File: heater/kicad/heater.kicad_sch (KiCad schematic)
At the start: 77 parts, among them J1 Conn_01x02_Pin, J2 Conn_01x02_Pin, J5 pcie_98, U1 ADS1261BIRHBT, U10 B0509XT-1WR3, U14 OPA333, U15 LTC1968, U16 OPA333, U2 ESD5344D-TP, U3 XC6206P332MR, U4 TPS7A2050PDBVR, U5 ADuM120N, U6 ADuM120N, U7 ADuM120N, U9 XC6206P332MR

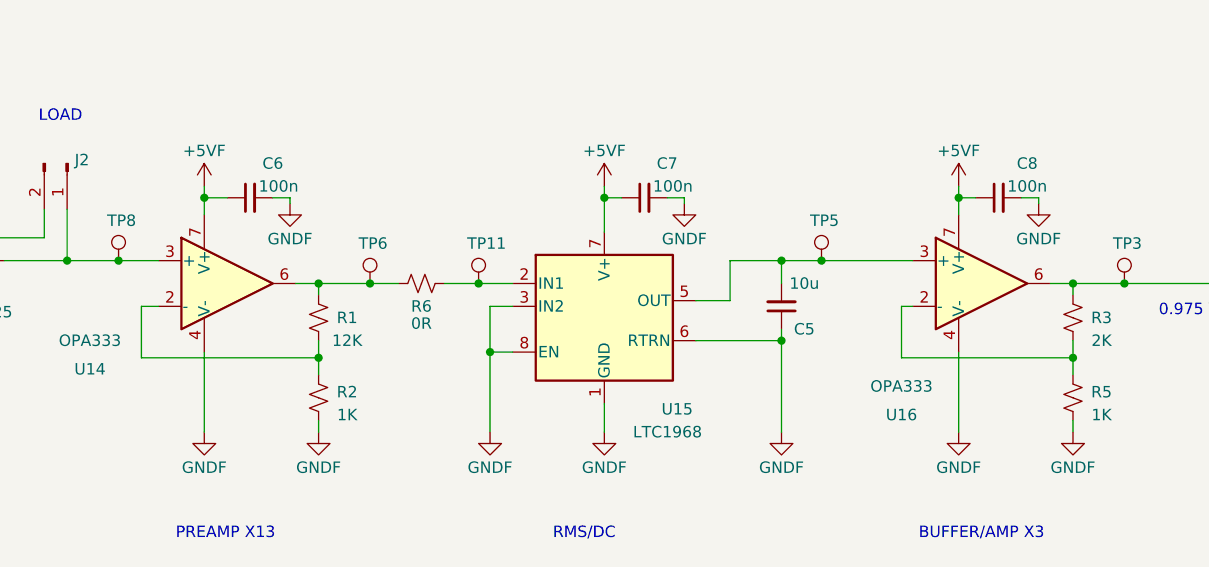
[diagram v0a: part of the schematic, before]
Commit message: Updated OPA333 pinout
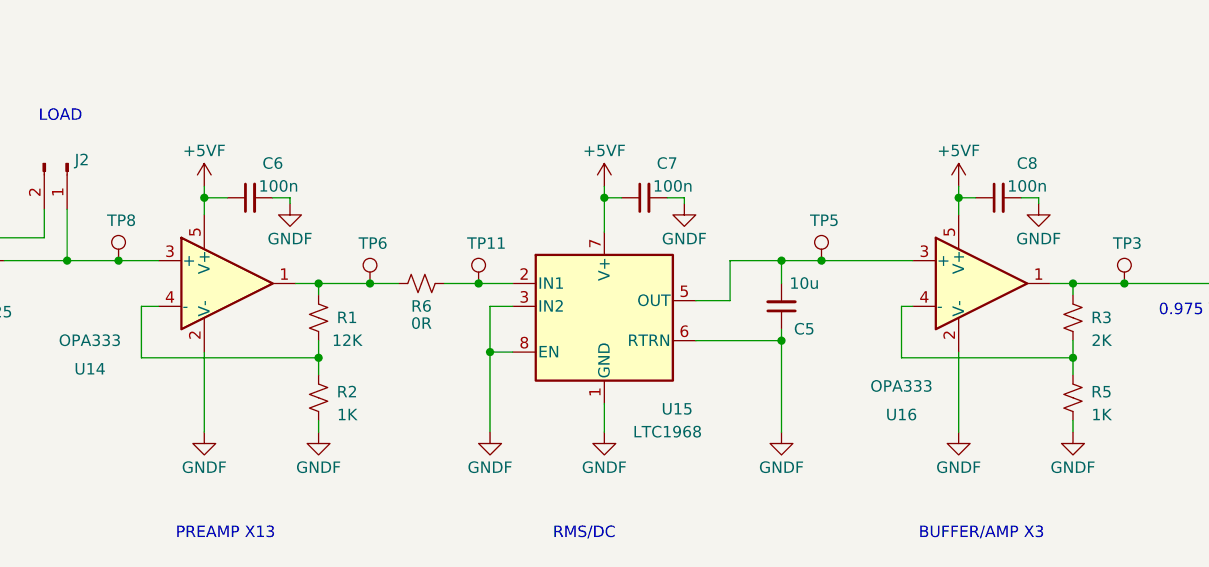
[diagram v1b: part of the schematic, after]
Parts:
- U14, U16: footprint Package_SO:SOIC-8_3.9x4.9mm_P1.27mm -> heater:SOT-23-5; symbol Amplifier_Operational:OPA333xxD -> Amplifier_Operational:OPA330xxDBV
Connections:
- net +5V: now also U14.5 (V+), U16.5 (V+); no longer U14.7 (V+), U16.7 (V+)
- net GND1: now also U14.2 (V-), U16.2 (V-); no longer U14.4 (V-), U16.4 (V-)
- net ISENSE: now also U16.1; no longer U16.6
- net at U14.1: now also R1.2, R6.2, TP6.1
- net at R1.1, R2.2: now also U14.4 (-); no longer U14.2 (-)
- net at R3.1, R5.2: now also U16.4 (-); no longer U16.2 (-)
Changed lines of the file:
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@@
     )
   )
-  (symbol (lib_id "Amplifier_Operational:OPA333xxD") (at 92.075 75.565 0) (unit 1)
+  (symbol (lib_id "Amplifier_Operational:OPA330xxDBV") (at 92.075 75.565 0) (unit 1)
     (in_bom yes) (on_board yes) (dnp no)
     (property "Reference" "U14" (at 76.835 85.09 0)
@@
       (effects (font (size 1.27 1.27)))
     )
-    (property "Footprint" "Package_SO:SOIC-8_3.9x4.9mm_P1.27mm" (at 89.535 80.645 0)
+    (property "Footprint" "heater:SOT-23-5" (at 89.535 80.645 0)
       (effects (font (size 1.27 1.27)) (justify left) hide)
     )
-    (property "Datasheet" "http://www.ti.com/lit/ds/symlink/opa333.pdf" (at 95.885 71.755 0)
-      (effects (font (size 1.27 1.27)) hide)
-    )
-    (pin "1")
-    (pin "2")
+    (property "Datasheet" "http://www.ti.com/lit/ds/symlink/opa330.pdf" (at 92.075 70.485 0)
+      (effects (font (size 1.27 1.27)) hide)
+    )
+    (pin "2")
+    (pin "5")
+    (pin "1")
     (pin "3")
     (pin "4")
-    (pin "5")
-    (pin "6")
-    (pin "7")
-    (pin "8")
     (instances
       (project "heater"
@@
     )
   )
-  (symbol (lib_id "Amplifier_Operational:OPA333xxD") (at 175.895 75.565 0) (unit 1)
+  (symbol (lib_id "Amplifier_Operational:OPA330xxDBV") (at 175.895 75.565 0) (unit 1)
     (in_bom yes) (on_board yes) (dnp no)
     (property "Reference" "U16" (at 167.005 90.17 0)
@@
       (effects (font (size 1.27 1.27)))
     )
-    (property "Footprint" "Package_SO:SOIC-8_3.9x4.9mm_P1.27mm" (at 173.355 80.645 0)
+    (property "Footprint" "heater:SOT-23-5" (at 173.355 80.645 0)
       (effects (font (size 1.27 1.27)) (justify left) hide)
     )
-    (property "Datasheet" "http://www.ti.com/lit/ds/symlink/opa333.pdf" (at 179.705 71.755 0)
-      (effects (font (size 1.27 1.27)) hide)
-    )
-    (pin "1")
-    (pin "2")
+    (property "Datasheet" "http://www.ti.com/lit/ds/symlink/opa330.pdf" (at 175.895 70.485 0)
+      (effects (font (size 1.27 1.27)) hide)
+    )
+    (pin "2")
+    (pin "5")
+    (pin "1")
     (pin "3")
     (pin "4")
-    (pin "5")
-    (pin "6")
-    (pin "7")
-    (pin "8")
-    (instances
-      (project "heater"
+    (instances
+      (project "heater"

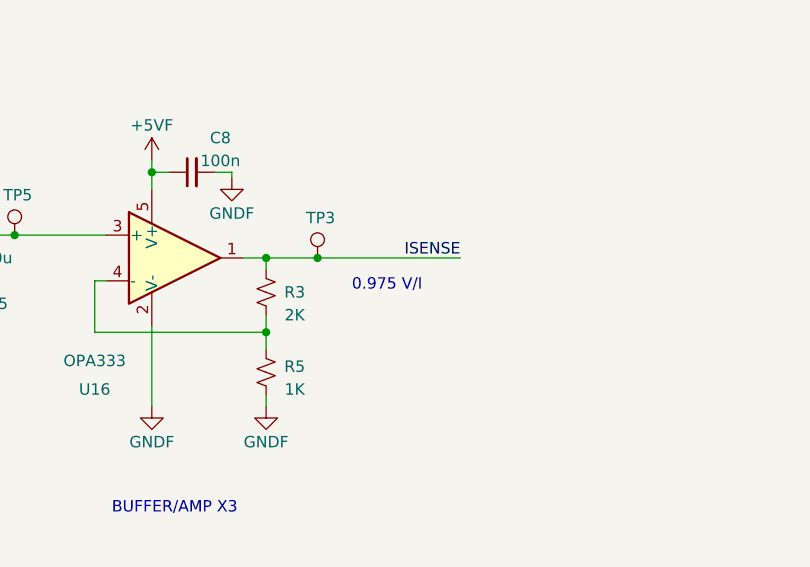
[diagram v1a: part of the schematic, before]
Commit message: Updated the heater schematic.
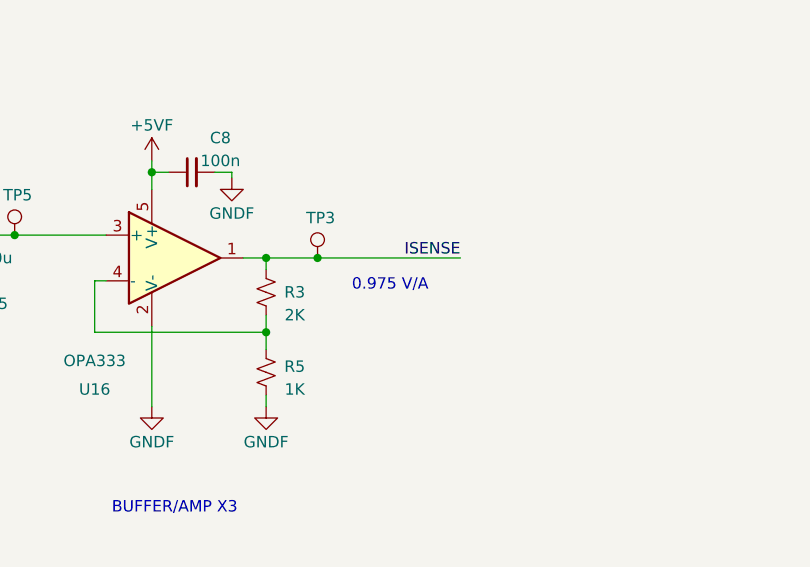
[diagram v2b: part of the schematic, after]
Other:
- note added: "0.975 V/A"
- note removed: "0.975 V/I"
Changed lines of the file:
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@@
     (effects (font (size 1.27 1.27)) (justify left bottom))
   )
-  (text "0.975 V/I" (at 195.58 79.375 0)
+  (text "0.975 V/A" (at 195.58 79.375 0)
     (effects (font (size 1.27 1.27)) (justify left bottom))
   )

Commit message: Updated heater schematic.
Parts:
- removed C12, C13, C30, C31, C44: 100n, Capacitor_SMD:C_0402_1005Metric, symbol Device:C_Small
- removed C17: 4n7, Capacitor_SMD:C_0402_1005Metric, symbol Device:C_Small
- removed C21, C35: 1u, Capacitor_SMD:C_0402_1005Metric, symbol Device:C_Small
- removed C22, C29, C32: 10u, Capacitor_SMD:C_0603_1608Metric, symbol Device:C_Small
- removed D3, D4: GRN, LED_SMD:LED_0603_1608Metric, symbol Device:LED
- removed R16, R28, R29: 51K, Resistor_SMD:R_0402_1005Metric, symbol Device:R_Small_US
- removed R18, R19, R21, R22: 47R, Resistor_SMD:R_0402_1005Metric, symbol Device:R_Small_US
- removed R24: 10K, Resistor_SMD:R_0402_1005Metric, symbol Device:R_Small_US
- removed R25, R26: 5K1, Resistor_SMD:R_0402_1005Metric, symbol Device:R_Small_US
- removed U1: ADS1261BIRHBT, heater:RHB0032E, symbol heater:ADS1261IRHBR
- removed U5, U6, U7: ADuM120N, Package_SO:SOIC-8_3.9x4.9mm_P1.27mm, symbol Isolator:ADuM120N
- removed U9: XC6206P332MR, Package_TO_SOT_SMD:SOT-23-3, symbol breakout:XC6206P332MR
- added C15, C16: 100n, Capacitor_SMD:C_0402_1005Metric, symbol Device:C_Small
- added R10, R7, R8, R9: ~, Resistor_SMD:R_0402_1005Metric, symbol Device:R_Small_US
- added R11: 12K, symbol Device:R_Small_US
- added R12: 1K, symbol Device:R_Small_US
- added U1: OPA333, heater:SOT-23-5, symbol Amplifier_Operational:OPA330xxDBV
- added U5: ISO1541, Package_SO:SOIC-8_3.9x4.9mm_P1.27mm, symbol Isolator:ISO1541
- added U8: ADS1115IDGS, Package_SO:TSSOP-10_3x3mm_P0.5mm, symbol heater:ADS1115IDGS
- C10, C11: value 1u -> 100n; LCSC C52923 -> C1525
- R15: value 51K -> 5K1; LCSC C25794 -> C25905
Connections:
- net +2V5A is gone; now on net +3V3: C10.2
- net +5VD is gone; now on net +5V: C1.2, C2.2, J5.B1 (Pin_b1), J5.B2 (Pin_b2), J5.B3 (Pin_b3), J5.B4 (Pin_b4), U3.3 (VIN)
- net +5V: now also U2.4 (D3), U2.5 (D4); no longer C24.2, C26.2, C27.2, C28.2, C6.1, C7.1, C8.1, C9.2, TP4.1, TP7.1, TP9.1, U10.5 (VOUT), U14.5 (V+), U15.7 (V+), U16.5 (V+), U4.1 (IN), U4.3 (EN), U4.5 (OUT)
- net GND: now also D2.1 (K), U5.4 (GND1); no longer C11.2, D1.1 (K), D2.2 (A), D5.1 (K)
- net GND1: now also C11.2, D1.1 (K), D5.1 (K), C15.2, C16.2, R12.1, U1.2 (V-), U5.5 (GND2), U8.1 (ADDR), U8.3 (GND)
- net +3V3: now reaches R15.1
- net +3V3: now also C3.2, C4.2, TP2.1, U3.2 (VOUT), U5.1 (VCC1)
- net PB7: now reaches U2.1 (D1)
- net PB7: now also J5.B7 (Pin_b7), R9.1, U5.2 (SDA1)
- net PB8: now reaches U2.2 (D2)
- net PB8: now also J5.B8 (Pin_b8), R10.1, U5.3 (SCL1)
- removed net +3V3D: C11.1, C3.2, C4.2, R15.2, R27.1, TP2.1, U3.2 (VOUT)
- net +5VA: no longer names the net of R23.1
- net +5VA: now also TP9.1, U1.1
- net ISENSE: no longer names the net of R3.2, TP3.1, U16.1
- net ISENSE: now also U1.3 (+), U8.4 (AIN0)
- net PA5: no longer names the net of J5.B28 (Pin_b28)
- net PA6: no longer names the net of J5.B21 (Pin_b21)
- net PA7: no longer names the net of J5.A27 (Pin_a27)
- net PB14: no longer names the net of J5.A16 (Pin_a16)
- new net: R8.1, U5.6 (SCL2), U8.10 (SCL)
- new net: R11.1, R12.2, U1.4 (-)
- new net: D2.2 (A), R15.2
- new net: R7.1, U5.7 (SDA2), U8.9 (SDA)
- new net +5VF: C11.1, C15.1, C16.1, C27.2, C28.2, C6.1, C7.1, C8.1, R10.2, R11.2, R27.1, R7.2, R8.2, R9.2, TP7.1, U1.5 (V+), U14.5 (V+), U15.7 (V+), U16.5 (V+), U4.5 (OUT), U5.8 (VCC2), U8.8 (VDD)
- new net 9VF: C24.2, C26.2, C9.2, TP4.1, U10.5 (VOUT), U4.1 (IN), U4.3 (EN)
- no-connect marks 92 -> 93
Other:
- note added: "CURRENT DETECTOR"
- note added: "LOW NOISE 5V"
- note added: "PWM CURRENT SENSOR"
- note added: "TODO: ADD PWD digital output."
- note added: "TODO: Add ADC addressing."
- note added: "TODO: Add test points"
- note added: "TODO: Change full scale to 4A."
- note added: "TODO: Consider adding a filter between analog and digital 5VF."
- note added: "TODO: Revisit bypass capacitors"
- note removed: "0.975 V/A"
- note removed: "ANALOG LOW NOISE 5V"
- note removed: "DIGITAL 3.3V"
- note removed: "TODO: Add DC/DC capacitors."
- moved on the sheet: C1, C14, C2, C24, C26, C27, C28, C3, C4, C5, C6, C7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

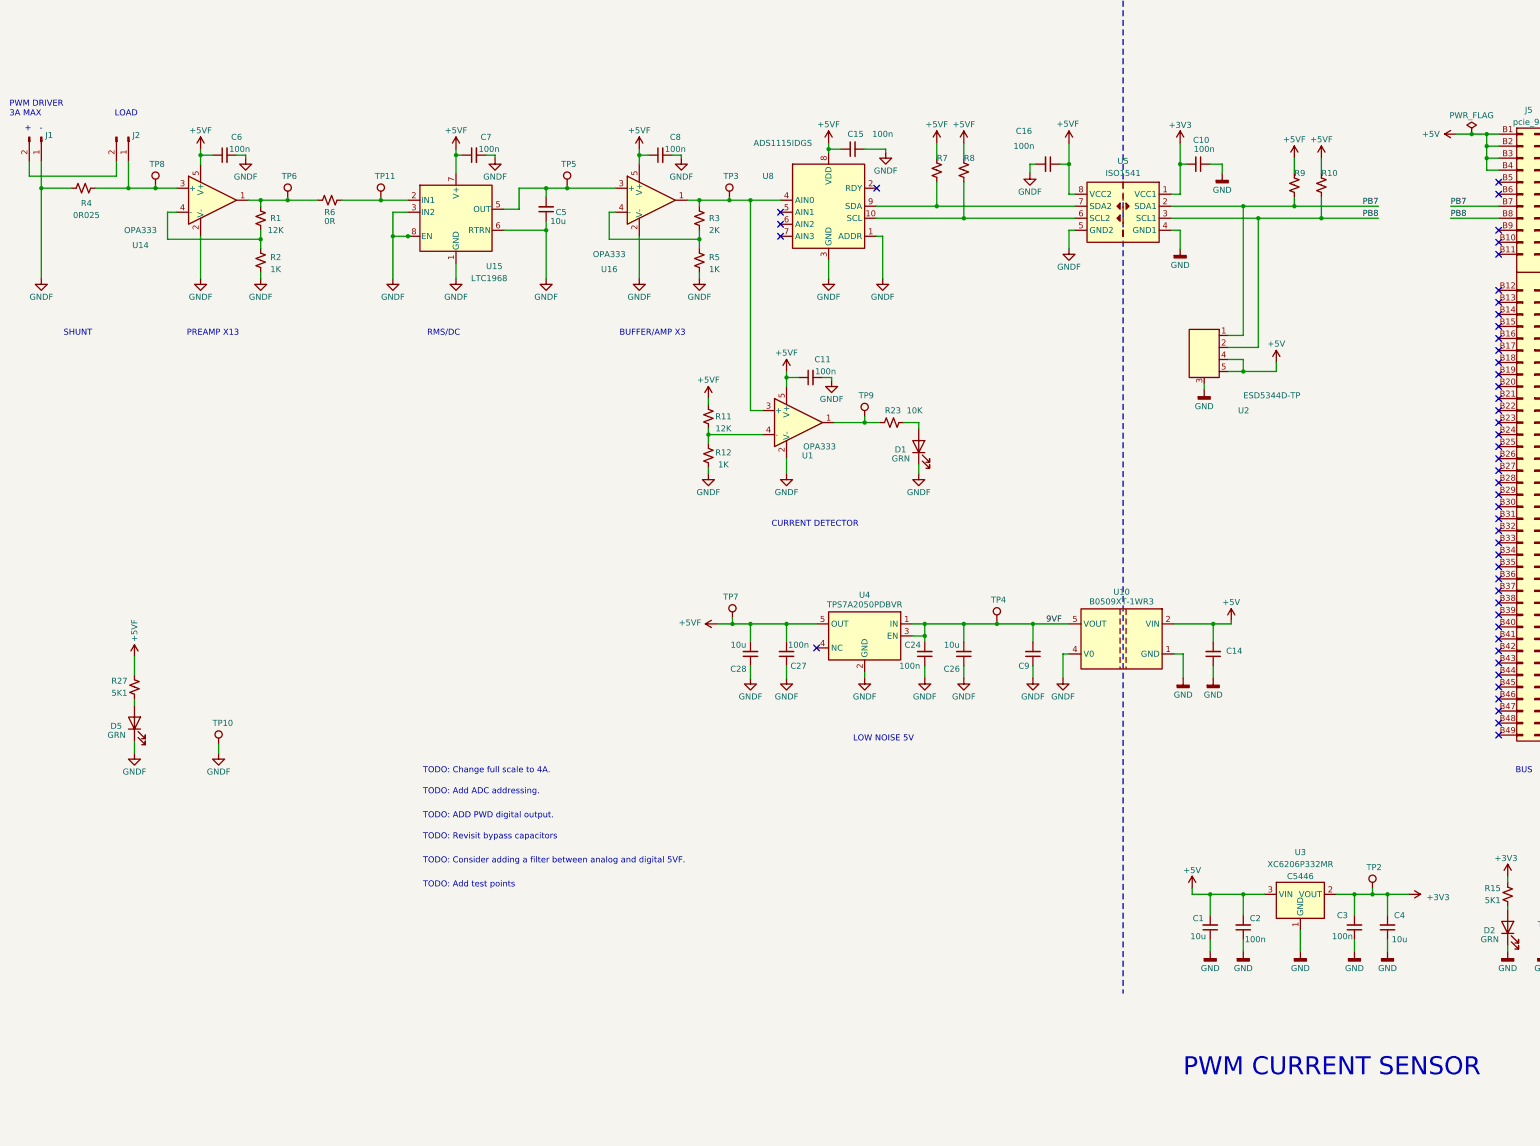
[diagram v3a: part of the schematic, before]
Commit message: Updated heater schematic
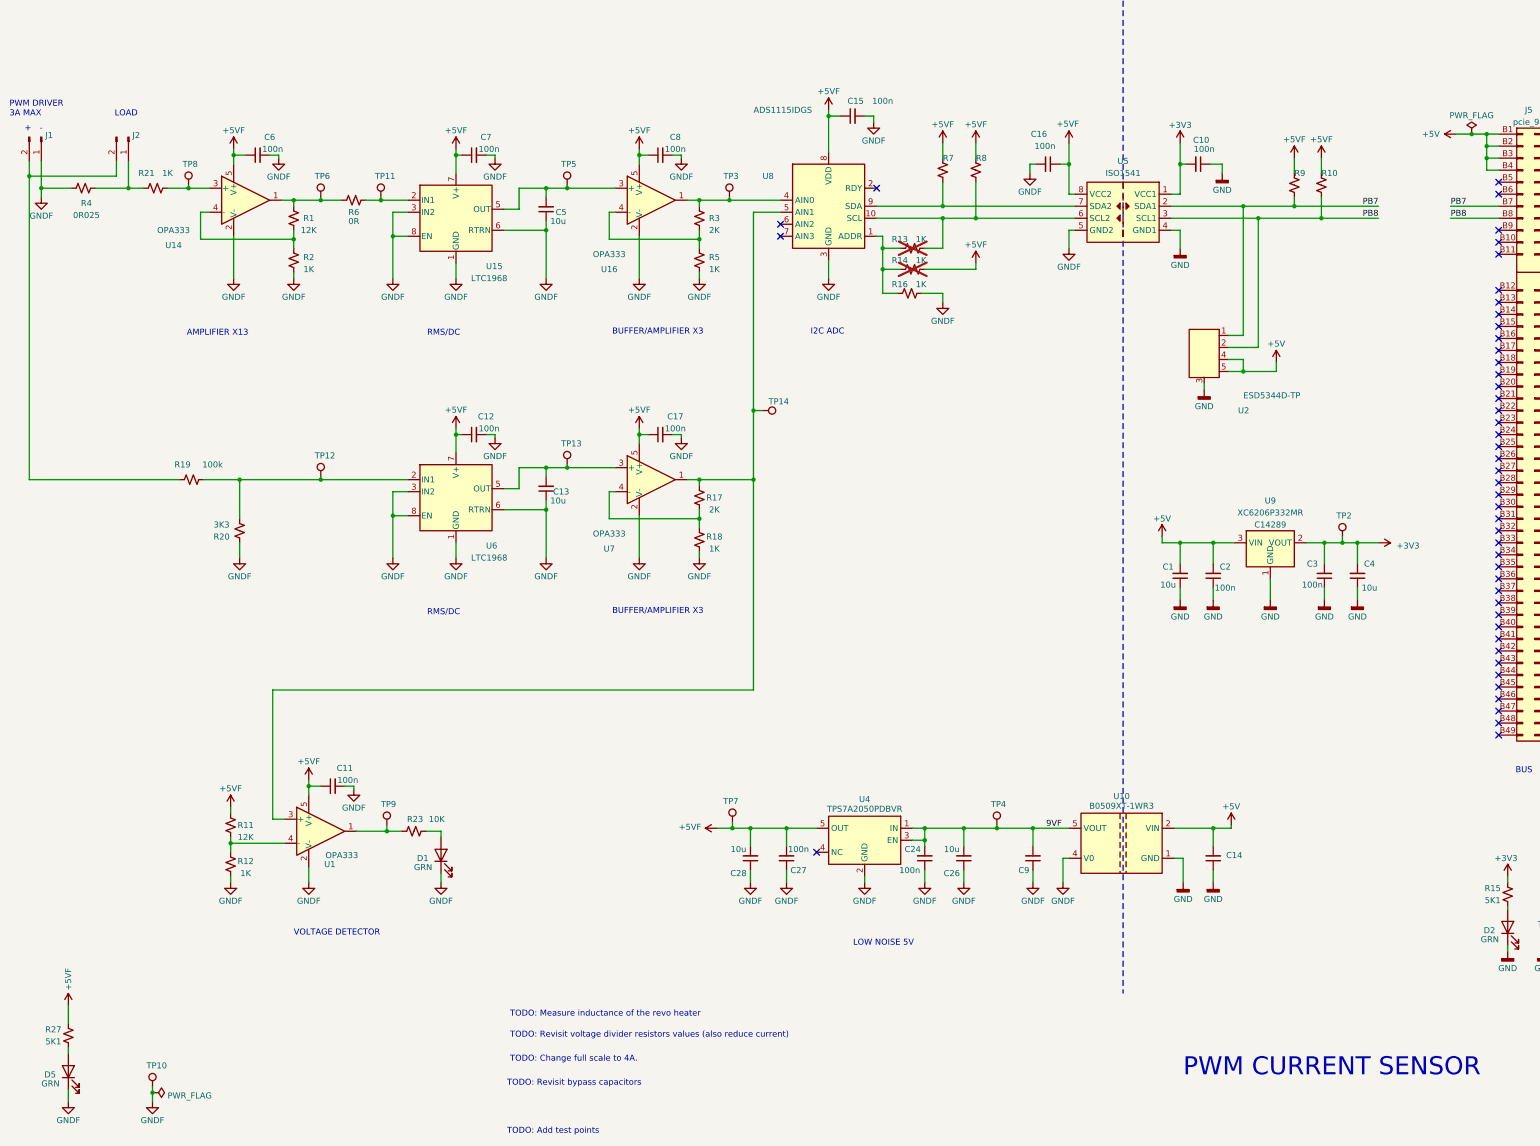
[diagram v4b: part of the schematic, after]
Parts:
- removed U3: XC6206P332MR, Package_TO_SOT_SMD:SOT-23-3, symbol breakout:XC6206P332MR
- added C12, C17: 100n, Capacitor_SMD:C_0402_1005Metric, symbol Device:C_Small
- added C13: 10u, Capacitor_SMD:C_0603_1608Metric, symbol Device:C_Small
- added R13, R14, R16: 1K, Resistor_SMD:R_0402_1005Metric, symbol Device:R_Small_US
- added R17: 2K, Resistor_SMD:R_0402_1005Metric, symbol Device:R_Small_US
- added R18, R21: 1K, symbol Device:R_Small_US
- added R19: 100k, symbol Device:R_Small_US
- added R20: 3K3, symbol Device:R_Small_US
- added TP12, TP13, TP14: TestPoint, common:Test_Pad, symbol common:TestPoint
- added U6: LTC1968, symbol heater:LTC1968
- added U7: OPA333, heater:SOT-23-5, symbol Amplifier_Operational:OPA330xxDBV
- added U9: XC6206P332MR, Package_TO_SOT_SMD:SOT-89-3, symbol common:XC6206P332MR
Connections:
- net +3V3: now also U9.2 (VOUT)
- net +5V: now also U9.3 (VIN)
- net +5VF: now also C12.1, C17.1, R14.2, U6.7 (V+), U7.5 (V+)
- net GND: now also U9.1 (GND)
- net GND1: now also C12.2, C13.1, C17.2, R16.2, R18.1, R20.2, U6.1 (GND), U6.3 (IN2), U6.6 (RTRN), U6.8 (EN), U7.2 (V-); no longer U8.1 (ADDR)
- net at R8.1, U5.6 (SCL2), U8.10 (SCL): now also R13.2
- net at TP8.1, U14.3 (+): now also R21.1; no longer J2.1 (Pin_1), R4.2
- net at J1.2 (Pin_2), J2.2 (Pin_2): now also R19.1
- net at R3.2, TP3.1, U16.1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: no longer U1.3 (+)
- net at U8.5 (AIN1): now also U1.3 (+), R17.2, TP14.1, U7.1
- new net: C13.2, TP13.1, U6.5 (OUT), U7.3 (+)
- new net: R13.1, R14.1, R16.1, U8.1 (ADDR)
- new net: R17.1, R18.2, U7.4 (-)
- new net: R19.2, R20.1, TP12.1, U6.2 (IN1)
- new net: J2.1 (Pin_1), R21.2, R4.2
- no-connect marks 93 -> 92
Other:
- note added: "AMPLIFIER X13"
- note added: "BUFFER/AMPLIFIER X3"
- note added: "I2C ADC"
- note added: "TODO: Measure inductance of the revo heater"
- note added: "TODO: Revisit voltage divider resistors values (also reduce current)"
- note added: "VOLTAGE DETECTOR"
- note removed: "BUFFER/AMP X3"
- note removed: "CURRENT DETECTOR"
- note removed: "PREAMP X13"
- note removed: "SHUNT"
- note removed: "TODO: ADD PWD digital output."
- note removed: "TODO: Add ADC addressing."
- note removed: "TODO: Consider adding a filter between analog and digital 5VF."
- moved on the sheet: C1, C11, C14, C15, C2, C24, C26, C27, C28, C3, C4, C6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
